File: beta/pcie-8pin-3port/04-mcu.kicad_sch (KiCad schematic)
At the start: 9 parts, among them SW1 BOOT, SW2 RESET, U1 ESP32-C6-MINI-1-N4

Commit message: Audit BETA electrical and pour pipeline
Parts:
- added R19: 10kΩ, cec-Resistor_SMD:R_0402_1005Metric, symbol cec-vendor:R_Small
- SW1, SW2: Manufacturer XKB -> XUNPU
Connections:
- net +3V3: now also R19.1
- net IO8_STRAP: now reaches U1.22 (IO8)
- net IO8_STRAP: now also R19.2
- no-connect marks 17 -> 16
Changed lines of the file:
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@@
 		(property "Value" "ESP32-C6-MINI-1-N4" (at 229.87 90.17 0) (effects (font (size 1.27 1.27))))
 		(property "Footprint" "cec-RF_Module:ESP32-C6-MINI-1" (at 229.87 128.27 0) (effects (font (size 1.27 1.27)) (hide yes)))
-		(property "Datasheet" "" (at 229.87 128.27 0) (effects (font (size 1.27 1.27)) (hide yes)))
+		(property "Datasheet" "https://documentation.espressif.com/esp32-c6-mini-1_mini-1u_datasheet_en.pdf" (at 229.87 128.27 0) (effects (font (size 1.27 1.27)) (hide yes)))
 		(property "Manufacturer" "Espressif Systems" (at 229.87 128.27 0) (effects (font (size 1.27 1.27)) (hide yes)))
 		(property "MPN" "ESP32-C6-MINI-1-N4" (at 229.87 128.27 0) (effects (font (size 1.27 1.27)) (hide yes)))
@@
 		(property "Value" "BOOT" (at 247.65 179.07 0) (effects (font (size 1.27 1.27))))
 		(property "Footprint" "cec-Button_Switch_SMD:TS-1088-AR02016" (at 247.65 182.88 0) (effects (font (size 1.27 1.27)) (hide yes)))
-		(property "Datasheet" "" (at 247.65 182.88 0) (effects (font (size 1.27 1.27)) (hide yes)))
-		(property "Manufacturer" "XKB" (at 247.65 182.88 0) (effects (font (size 1.27 1.27)) (hide yes)))
+		(property "Datasheet" "https://www.lcsc.com/datasheet/C720477.pdf" (at 247.65 182.88 0) (effects (font (size 1.27 1.27)) (hide yes)))
+		(property "Manufacturer" "XUNPU" (at 247.65 182.88 0) (effects (font (size 1.27 1.27)) (hide yes)))
 		(property "MPN" "TS-1088-AR02016" (at 247.65 182.88 0) (effects (font (size 1.27 1.27)) (hide yes)))
 		(property "LCSC" "C720477" (at 247.65 182.88 0) (effects (font (size 1.27 1.27)) (hide yes)))
@@
 		(property "Value" "RESET" (at 267.97 179.07 0) (effects (font (size 1.27 1.27))))
 		(property "Footprint" "cec-Button_Switch_SMD:TS-1088-AR02016" (at 267.97 182.88 0) (effects (font (size 1.27 1.27)) (hide yes)))
-		(property "Datasheet" "" (at 267.97 182.88 0) (effects (font (size 1.27 1.27)) (hide yes)))
-		(property "Manufacturer" "XKB" (at 267.97 182.88 0) (effects (font (size 1.27 1.27)) (hide yes)))
+		(property "Datasheet" "https://www.lcsc.com/datasheet/C720477.pdf" (at 267.97 182.88 0) (effects (font (size 1.27 1.27)) (hide yes)))
+		(property "Manufacturer" "XUNPU" (at 267.97 182.88 0) (effects (font (size 1.27 1.27)) (hide yes)))
 		(property "MPN" "TS-1088-AR02016" (at 267.97 182.88 0) (effects (font (size 1.27 1.27)) (hide yes)))
 		(property "LCSC" "C720477" (at 267.97 182.88 0) (effects (font (size 1.27 1.27)) (hide yes)))
@@
 	(no_connect (at 218.44 143.51))
 	(no_connect (at 218.44 146.05))
-	(no_connect (at 218.44 148.59))
-	(no_connect (at 241.3 154.94))
+		(no_connect (at 241.3 154.94))
 	(no_connect (at 241.3 152.4))
 	(no_connect (at 241.3 149.86))
@@
 		(stroke (width 0) (type default)))
 	(label "GPIO0" (at 210.82 115.57 270) (effects (font (size 1.27 1.27)) (justify left bottom)))
+	(wire (pts (xy 218.44 148.59) (xy 214.63 148.59))
+		(stroke (width 0) (type default)))
+	(label "IO8_STRAP" (at 214.63 148.59 180) (effects (font (size 1.27 1.27)) (justify right bottom)))
+	(symbol
+		(lib_id "cec-vendor:R_Small")
+		(at 196.85 160.02 0)
+		(unit 1)
+		(exclude_from_sim no)
+		(in_bom yes)
+		(on_board yes)
+		(dnp no)
+		(fields_autoplaced yes)
+		(property "Reference" "R19" (at 196.85 153.67 0) (effects (font (size 1.27 1.27))))
+		(property "Value" "10kΩ" (at 196.85 166.37 0) (effects (font (size 1.27 1.27))))
+		(property "Footprint" "cec-Resistor_SMD:R_0402_1005Metric" (at 196.85 160.02 0) (effects (font (size 1.27 1.27)) (hide yes)))
+		(property "Datasheet" "https://www.lcsc.com/product-detail/C25744.html" (at 196.85 160.02 0) (effects (font (size 1.27 1.27)) (hide yes)))
+		(property "Manufacturer" "UNI-ROYAL" (at 196.85 160.02 0) (effects (font (size 1.27 1.27)) (hide yes)))
+		(property "MPN" "0402WGF1002TCE" (at 196.85 160.02 0) (effects (font (size 1.27 1.27)) (hide yes)))
+		(property "LCSC" "C25744" (at 196.85 160.02 0) (effects (font (size 1.27 1.27)) (hide yes)))
+		(property "Description" "ESP32-C6 GPIO8 download-strap pull-up" (at 196.85 160.02 0) (effects (font (size 1.27 1.27)) (hide yes)))
+		(property "Note" "10 kohm follows Espressif ESP32-C6-DevKitC-1; GPIO8 must be high with GPIO9 low for joint download boot" (at 196.85 160.02 0) (effects (font (size 1.27 1.27)) (hide yes)))
+		(pin "1")
+		(pin "2")
+		(instances
+			(project "pcie8pin-3port-module"
+				(path "/a8ecf94e-f41a-4523-8cf1-1d72f47f3e7e/83ceb2d1-e50f-4838-831a-71136b7d1260" (reference "R19") (unit 1))
+			)
+		)
+	)
+	(wire (pts (xy 196.85 157.48) (xy 196.85 154.94))
+		(stroke (width 0) (type default)))
+	(symbol
+		(lib_id "cec-power:+3V3")
+		(at 196.85 154.94 0)
+		(unit 1)
+		(exclude_from_sim no)
+		(in_bom yes)
+		(on_board yes)
+		(dnp no)
+		(property "Reference" "#PWR0799" (at 196.85 152.4 0) (effects (font (size 1.27 1.27)) (hide yes)))
+		(property "Value" "+3V3" (at 196.85 158.75 0) (effects (font (size 1.27 1.27))))
+		(pin "1")
+		(instances
+			(project "pcie8pin-3port-module"
+				(path "/a8ecf94e-f41a-4523-8cf1-1d72f47f3e7e/83ceb2d1-e50f-4838-831a-71136b7d1260" (reference "#PWR0799") (unit 1))
+			)
+		)
+	)
+	(wire (pts (xy 196.85 162.56) (xy 196.85 165.1))
+		(stroke (width 0) (type default)))
+	(label "IO8_STRAP" (at 196.85 165.1 270) (effects (font (size 1.27 1.27)) (justify left bottom)))
 	(sheet_instances
 		(path "/83ceb2d1-e50f-4838-831a-71136b7d1260"

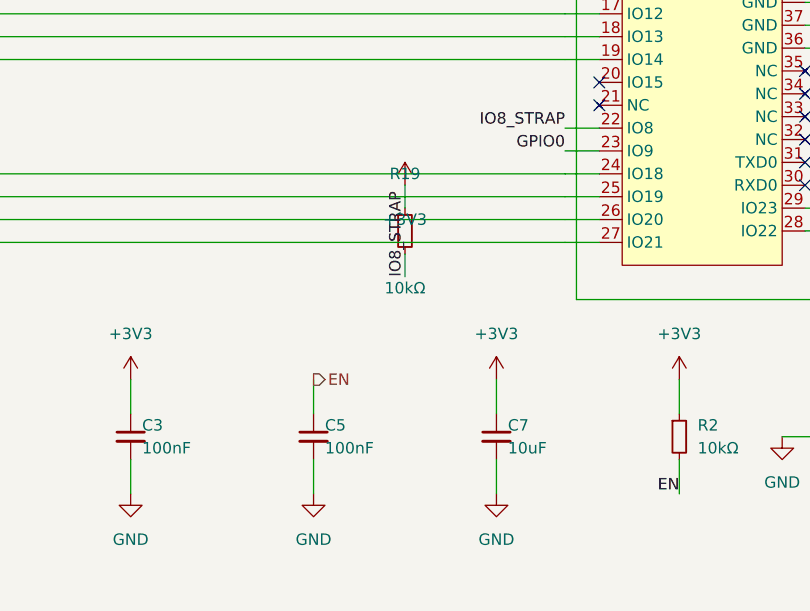
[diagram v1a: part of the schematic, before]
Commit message: Audit BETA power designs and harden PCB pipeline
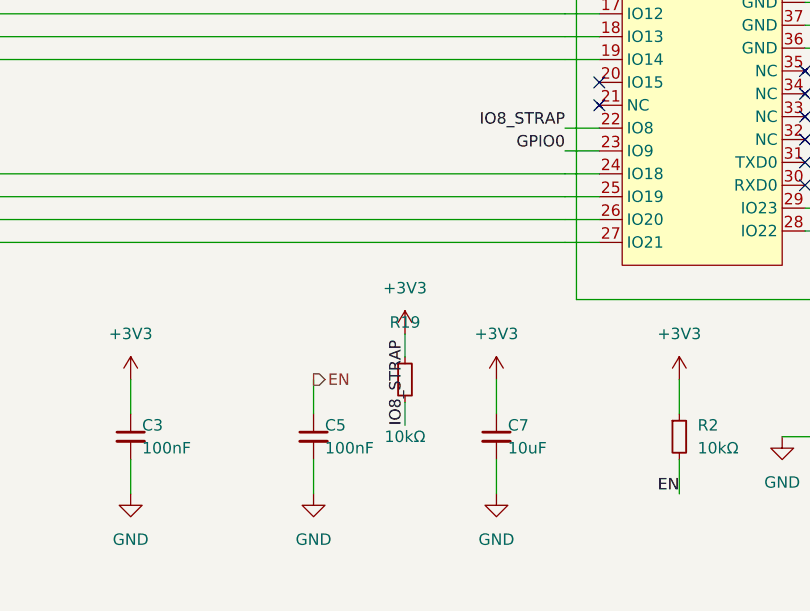
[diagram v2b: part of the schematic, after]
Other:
- moved on the sheet: R19
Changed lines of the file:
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@@
 	(symbol
 		(lib_id "cec-vendor:R_Small")
-		(at 196.85 160.02 0)
+		(at 196.85 176.53 0)
 		(unit 1)
 		(exclude_from_sim no)
@@
 		(dnp no)
 		(fields_autoplaced yes)
-		(property "Reference" "R19" (at 196.85 153.67 0) (effects (font (size 1.27 1.27))))
-		(property "Value" "10kΩ" (at 196.85 166.37 0) (effects (font (size 1.27 1.27))))
-		(property "Footprint" "cec-Resistor_SMD:R_0402_1005Metric" (at 196.85 160.02 0) (effects (font (size 1.27 1.27)) (hide yes)))
-		(property "Datasheet" "https://www.lcsc.com/product-detail/C25744.html" (at 196.85 160.02 0) (effects (font (size 1.27 1.27)) (hide yes)))
-		(property "Manufacturer" "UNI-ROYAL" (at 196.85 160.02 0) (effects (font (size 1.27 1.27)) (hide yes)))
-		(property "MPN" "0402WGF1002TCE" (at 196.85 160.02 0) (effects (font (size 1.27 1.27)) (hide yes)))
-		(property "LCSC" "C25744" (at 196.85 160.02 0) (effects (font (size 1.27 1.27)) (hide yes)))
-		(property "Description" "ESP32-C6 GPIO8 download-strap pull-up" (at 196.85 160.02 0) (effects (font (size 1.27 1.27)) (hide yes)))
-		(property "Note" "10 kohm follows Espressif ESP32-C6-DevKitC-1; GPIO8 must be high with GPIO9 low for joint download boot" (at 196.85 160.02 0) (effects (font (size 1.27 1.27)) (hide yes)))
+		(property "Reference" "R19" (at 196.85 170.18 0) (effects (font (size 1.27 1.27))))
+		(property "Value" "10kΩ" (at 196.85 182.88 0) (effects (font (size 1.27 1.27))))
+		(property "Footprint" "cec-Resistor_SMD:R_0402_1005Metric" (at 196.85 176.53 0) (effects (font (size 1.27 1.27)) (hide yes)))
+		(property "Datasheet" "https://www.lcsc.com/product-detail/C25744.html" (at 196.85 176.53 0) (effects (font (size 1.27 1.27)) (hide yes)))
+		(property "Manufacturer" "UNI-ROYAL" (at 196.85 176.53 0) (effects (font (size 1.27 1.27)) (hide yes)))
+		(property "MPN" "0402WGF1002TCE" (at 196.85 176.53 0) (effects (font (size 1.27 1.27)) (hide yes)))
+		(property "LCSC" "C25744" (at 196.85 176.53 0) (effects (font (size 1.27 1.27)) (hide yes)))
+		(property "Description" "ESP32-C6 GPIO8 download-strap pull-up" (at 196.85 176.53 0) (effects (font (size 1.27 1.27)) (hide yes)))
+		(property "Note" "10 kohm follows Espressif ESP32-C6-DevKitC-1; GPIO8 must be high with GPIO9 low for joint download boot" (at 196.85 176.53 0) (effects (font (size 1.27 1.27)) (hide yes)))
 		(pin "1")
 		(pin "2")
@@
 		)
 	)
-	(wire (pts (xy 196.85 157.48) (xy 196.85 154.94))
+	(wire (pts (xy 196.85 173.99) (xy 196.85 171.45))
 		(stroke (width 0) (type default)))
 	(symbol
 		(lib_id "cec-power:+3V3")
-		(at 196.85 154.94 0)
+		(at 196.85 171.45 0)
 		(unit 1)
 		(exclude_from_sim no)
@@
 		(on_board yes)
 		(dnp no)
-		(property "Reference" "#PWR0799" (at 196.85 152.4 0) (effects (font (size 1.27 1.27)) (hide yes)))
-		(property "Value" "+3V3" (at 196.85 158.75 0) (effects (font (size 1.27 1.27))))
+		(property "Reference" "#PWR0799" (at 196.85 168.91 0) (effects (font (size 1.27 1.27)) (hide yes)))
+		(property "Value" "+3V3" (at 196.85 166.37 0) (effects (font (size 1.27 1.27))))
 		(pin "1")
 		(instances
@@
 		)
 	)
-	(wire (pts (xy 196.85 162.56) (xy 196.85 165.1))
+	(wire (pts (xy 196.85 179.07) (xy 196.85 181.61))
 		(stroke (width 0) (type default)))
-	(label "IO8_STRAP" (at 196.85 165.1 270) (effects (font (size 1.27 1.27)) (justify left bottom)))
+	(label "IO8_STRAP" (at 196.85 181.61 270) (effects (font (size 1.27 1.27)) (justify left bottom)))
 	(sheet_instances
 		(path "/83ceb2d1-e50f-4838-831a-71136b7d1260"

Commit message: pipeline: integrate route-aware physical design flow
Generalize critical-first placement and routing, future-congestion and power-authority planning, route provenance, process watchdogs, fab/thermal validation, dashboard review, and XFCN integration. Add the supporting board contracts, component libraries, documentation, and regression coverage.
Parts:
- C41: LCSC (none) -> C1525; MPN (none) -> CL05B104KO5NNNC; Manufacturer (none) -> Samsung
- C7: value 10uF -> 4.7uF; LCSC C15850 -> C1779; MPN CL21A106KAYNNNE -> CL21A475KAQNNNE; Note (none) -> LP5907 output bulk; 4.7uF keeps the complete nominal +3V3 n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
- R13: LCSC (none) -> C25744; MPN (none) -> 0402WGF1002TCE; Manufacturer (none) -> UNI-ROYAL
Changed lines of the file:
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@@
 		(fields_autoplaced yes)
 		(property "Reference" "C7" (at 208.28 181.61 0) (effects (font (size 1.27 1.27)) (justify left)))
-		(property "Value" "10uF" (at 208.28 184.15 0) (effects (font (size 1.27 1.27)) (justify left)))
+		(property "Value" "4.7uF" (at 208.28 184.15 0) (effects (font (size 1.27 1.27)) (justify left)))
 		(property "Footprint" "cec-Capacitor_SMD:C_0805_2012Metric" (at 207.01 182.88 0) (effects (font (size 1.27 1.27)) (hide yes)))
-		(property "Datasheet" "" (at 207.01 182.88 0) (effects (font (size 1.27 1.27)) (hide yes)))
+		(property "Datasheet" "https://product.samsungsem.com/mlcc/CL21A475KAQNNN.do" (at 207.01 182.88 0) (effects (font (size 1.27 1.27)) (hide yes)))
 		(property "Manufacturer" "Samsung" (at 207.01 182.88 0) (effects (font (size 1.27 1.27)) (hide yes)))
-		(property "MPN" "CL21A106KAYNNNE" (at 207.01 182.88 0) (effects (font (size 1.27 1.27)) (hide yes)))
-		(property "LCSC" "C15850" (at 207.01 182.88 0) (effects (font (size 1.27 1.27)) (hide yes)))
+		(property "MPN" "CL21A475KAQNNNE" (at 207.01 182.88 0) (effects (font (size 1.27 1.27)) (hide yes)))
+		(property "LCSC" "C1779" (at 207.01 182.88 0) (effects (font (size 1.27 1.27)) (hide yes)))
+		(property "Note" "LP5907 output bulk; 4.7uF keeps the complete nominal +3V3 network inside the 10uF documented application range." (at 207.01 182.88 0) (effects (font (size 1.27 1.27)) (hide yes)))
 		(pin "1")
 		(pin "2")
@@
 		(property "Value" "100nF" (at 200.66 116.84 0) (effects (font (size 1.27 1.27))))
 		(property "Footprint" "cec-Capacitor_SMD:C_0402_1005Metric" (at 200.66 110.49 0) (effects (font (size 1.27 1.27)) (hide yes)))
-		(property "Datasheet" "" (at 200.66 110.49 0) (effects (font (size 1.27 1.27)) (hide yes)))
+		(property "Datasheet" "https://product.samsungsem.com/mlcc/CL05B104KO5NNN.do" (at 200.66 110.49 0) (effects (font (size 1.27 1.27)) (hide yes)))
+		(property "Manufacturer" "Samsung" (at 200.66 110.49 0) (effects (font (size 1.27 1.27)) (hide yes)))
+		(property "MPN" "CL05B104KO5NNNC" (at 200.66 110.49 0) (effects (font (size 1.27 1.27)) (hide yes)))
+		(property "LCSC" "C1525" (at 200.66 110.49 0) (effects (font (size 1.27 1.27)) (hide yes)))
 		(pin "1")
 		(pin "2")
@@
 		(property "Value" "10kΩ" (at 210.82 116.84 0) (effects (font (size 1.27 1.27))))
 		(property "Footprint" "cec-Resistor_SMD:R_0402_1005Metric" (at 210.82 110.49 0) (effects (font (size 1.27 1.27)) (hide yes)))
-		(property "Datasheet" "" (at 210.82 110.49 0) (effects (font (size 1.27 1.27)) (hide yes)))
+		(property "Datasheet" "https://www.lcsc.com/product-detail/C25744.html" (at 210.82 110.49 0) (effects (font (size 1.27 1.27)) (hide yes)))
+		(property "Manufacturer" "UNI-ROYAL" (at 210.82 110.49 0) (effects (font (size 1.27 1.27)) (hide yes)))
+		(property "MPN" "0402WGF1002TCE" (at 210.82 110.49 0) (effects (font (size 1.27 1.27)) (hide yes)))
+		(property "LCSC" "C25744" (at 210.82 110.49 0) (effects (font (size 1.27 1.27)) (hide yes)))
 		(pin "1")
 		(pin "2")
